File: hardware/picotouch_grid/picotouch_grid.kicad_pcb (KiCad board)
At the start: 2 copper layers, 180 x 110 mm, 127 parts, among them U1 Pico, U2 TS20, U3 TS20

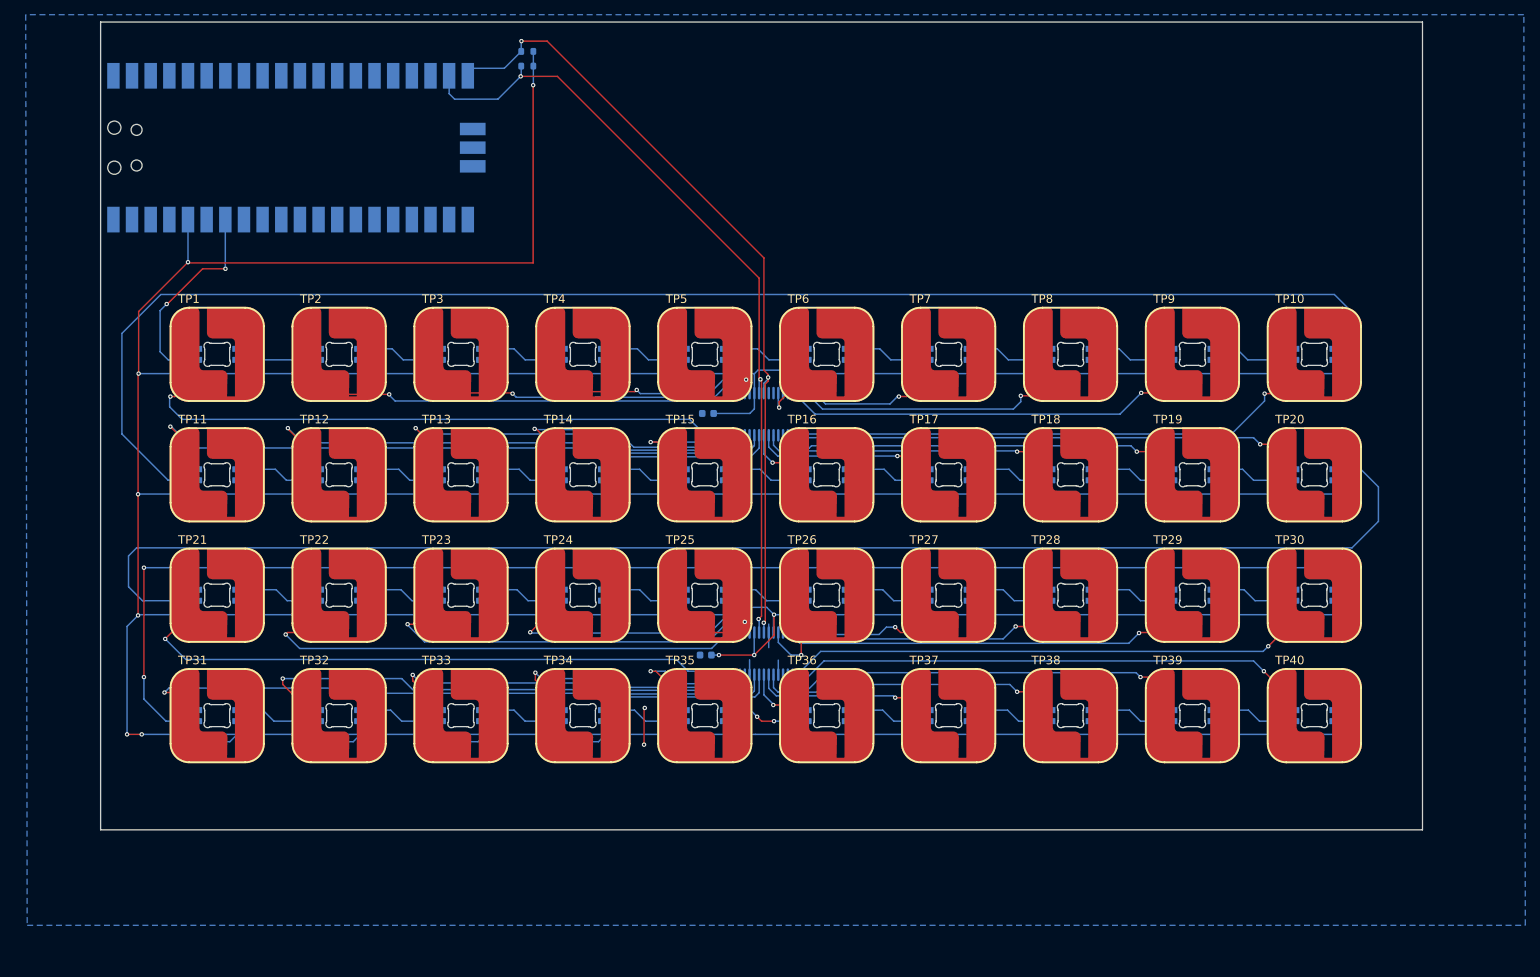
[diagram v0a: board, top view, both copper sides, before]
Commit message: added jlcpcb dru rules from "KiCad-DesignRules"
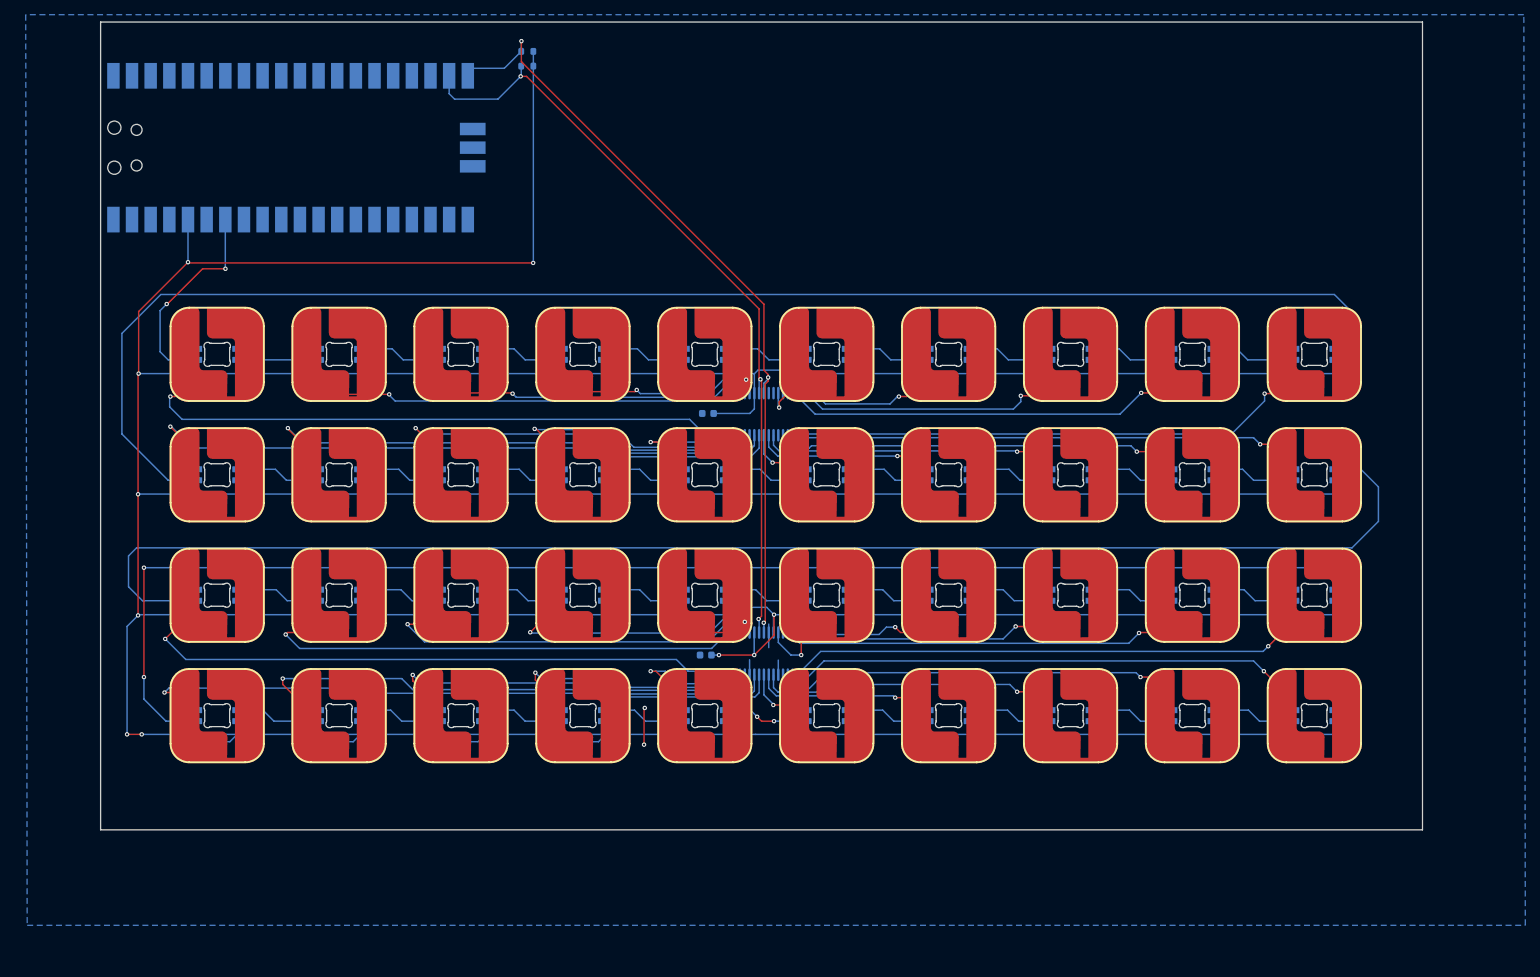
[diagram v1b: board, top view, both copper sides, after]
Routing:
- net /TOUCH_SDA: track 108.7 -> 106.3 mm
- net /TOUCH_SCL: track 110.7 -> 108.6 mm

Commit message: pcb: added midi in/out, pwm audio out
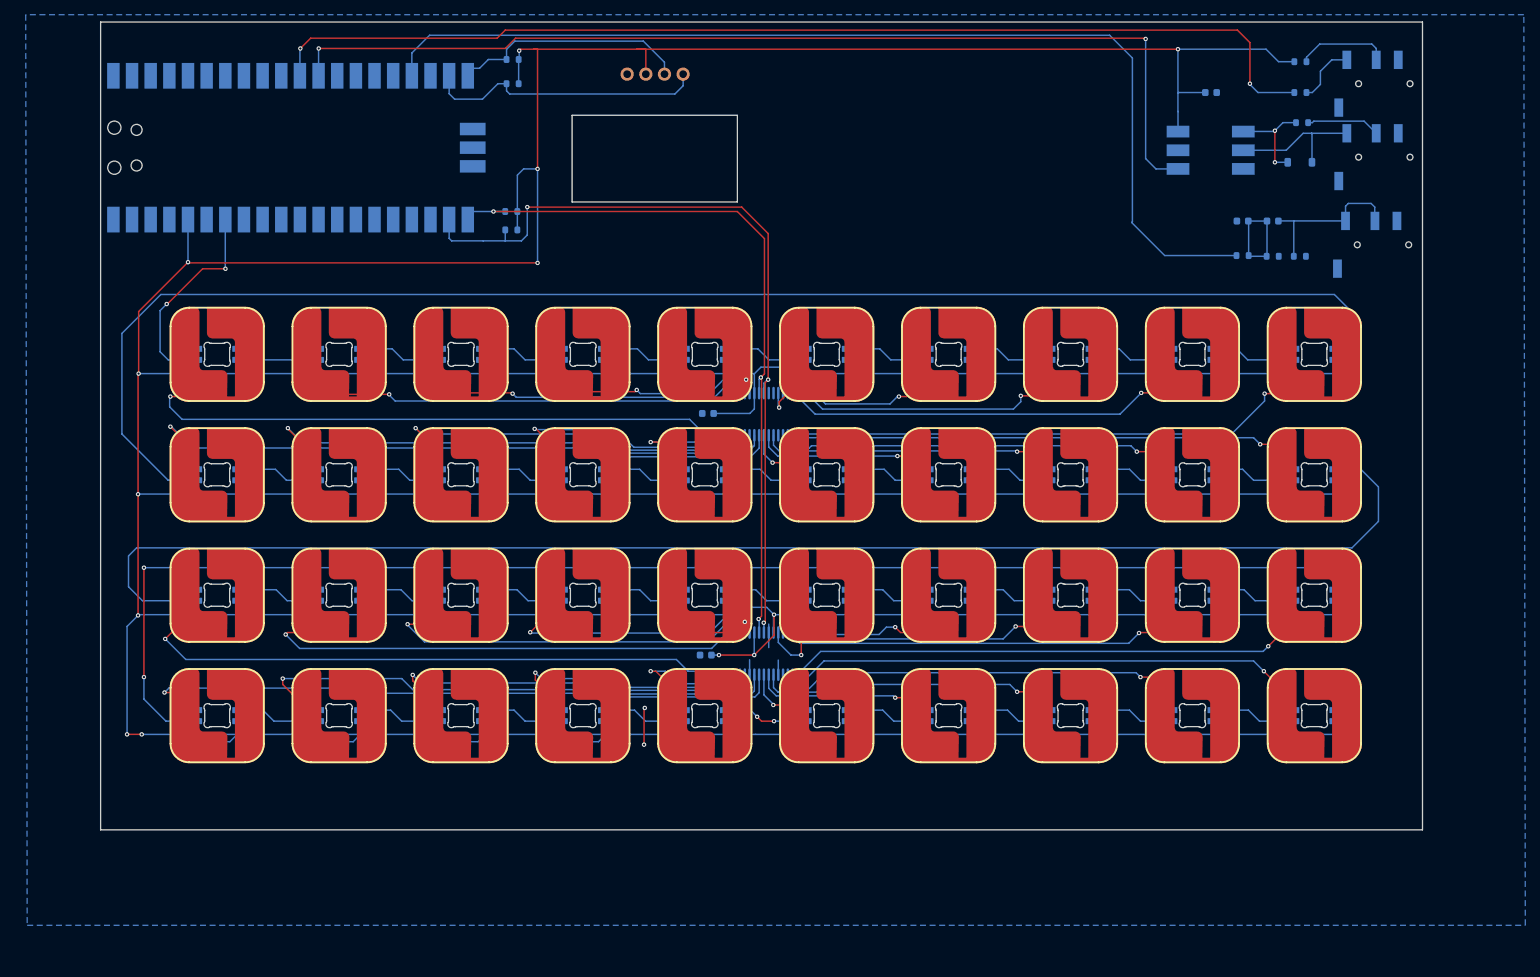
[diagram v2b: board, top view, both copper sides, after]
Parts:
- added C43: 100n, Capacitor_SMD:C_0603_1608Metric, B.Cu at (188.2, 34.6)
- added C44: 100n, Capacitor_SMD:C_0603_1608Metric, B.Cu at (192.5, 52.1)
- added C45: 47uF, Capacitor_SMD:C_0603_1608Metric, B.Cu at (196.6, 52.1)
- added D1: 1N4148, Diode_SMD:D_SOD-123, B.Cu at (200.3, 44.1)
- added DISP1: HS96L03W2C03, todbot_stuff:OLED-TH_under_L27.8-W27.2-P2.54_C9900033791, F.Cu at (112.5, 32.1)
- added J1: TRRS, Keebio-Parts:TRRS-PJ-320D, B.Cu at (216.9, 43.4)
- added J2: TRRS, Keebio-Parts:TRRS-PJ-320D, B.Cu at (216.9, 33.4)
- added J3: TRRS, Keebio-Parts:TRRS-PJ-320D, B.Cu at (216.7, 55.3)
- added R10: 1.8k, Resistor_SMD:R_0603_1608Metric, B.Cu at (200.3, 56.9)
- added R3: 4.7k, Resistor_SMD:R_0603_1608Metric, B.Cu at (92.9, 53.3)
- added R4: 4.7k, Resistor_SMD:R_0603_1608Metric, B.Cu at (92.9, 50.8)
- added R5: 200, Resistor_SMD:R_0603_1608Metric, B.Cu at (200.6, 38.7)
- added R6: 33, Resistor_SMD:R_0603_1608Metric, B.Cu at (200.4, 30.4)
- added R7: 10, Resistor_SMD:R_0603_1608Metric, B.Cu at (200.4, 34.6)
- added R8: 200, Resistor_SMD:R_0603_1608Metric, B.Cu at (192.5, 56.8)
- added R9: 100, Resistor_SMD:R_0603_1608Metric, B.Cu at (196.6, 56.9)
- added U5: H11L1, Package_DIP:DIP-6_W8.89mm_SMDSocket_LongPads, B.Cu at (188.2, 42.5)
- moved R1 3.12 mm to (93.1, 33.4)
- moved R2 2.28 mm to (93.1, 30.1)
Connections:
- R1 pad 2: /TOUCH_SDA -> /DISP_SDA
- R2 pad 2: /TOUCH_SCL -> /DISP_SCL
- U1 pad 11: unconnected-(U1-GPIO8-Pad11) -> /MIDI_OUT
- U1 pad 12: unconnected-(U1-GPIO9-Pad12) -> /MIDI_IN
- U1 pad 17: unconnected-(U1-GPIO13-Pad17) -> /PWM_AUDIO
- U1 pad 19: /TOUCH_SDA -> /DISP_SDA
- U1 pad 20: /TOUCH_SCL -> /DISP_SCL
- U1 pad 21: unconnected-(U1-GPIO16-Pad21) -> /TOUCH_SDA
- U1 pad 22: unconnected-(U1-GPIO17-Pad22) -> /TOUCH_SCL
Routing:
- net /MIDI_OUT: track 0.00 -> 147.9 mm, vias 0 -> 2
- net /PWM_AUDIO: track 0.00 -> 143.0 mm
- net +3V3: track 953.7 -> 1096.6 mm, vias 10 -> 13
- net /MIDI_IN: track 0.00 -> 139.1 mm, vias 0 -> 2
- net /DISP_SDA: track 0.00 -> 37.7 mm
- net /DISP_SCL: track 0.00 -> 32.0 mm
- net /AUDIO_OUT: track 0.00 -> 22.2 mm
- net Net-(D1-A): track 0.00 -> 19.2 mm
- net Net-(C44-Pad1): track 0.00 -> 14.6 mm
- net Net-(D1-K): track 0.00 -> 13.7 mm, vias 0 -> 2
- net Net-(J2-RING1): track 0.00 -> 12.6 mm
- net Net-(J1-RING1): track 0.00 -> 10.0 mm
- net Net-(J2-TIP): track 0.00 -> 8.40 mm
- net /TOUCH_SDA: track 106.3 -> 99.9 mm
- net /TOUCH_SCL: track 108.6 -> 110.9 mm
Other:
- outline, holes or cut-outs redrawn

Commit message: pcb: add more buttons, clean up layout of sch & pcb
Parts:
- added H1: MountingHole, MountingHole:MountingHole_2.7mm_M2.5, F.Cu at (34.0, 34.0)
- added H2: MountingHole, MountingHole:MountingHole_2.7mm_M2.5, F.Cu at (34.0, 136.0)
- added H3: MountingHole, MountingHole:MountingHole_2.7mm_M2.5, F.Cu at (206.0, 34.0)
- added H4: MountingHole, MountingHole:MountingHole_2.7mm_M2.5, F.Cu at (206.0, 136.0)
- added R11: 1M, Resistor_SMD:R_0603_1608Metric, B.Cu at (47.1, 33.6)
- added R12: 1M, Resistor_SMD:R_0603_1608Metric, B.Cu at (49.9, 33.6)
- added R13: 1M, Resistor_SMD:R_0603_1608Metric, B.Cu at (52.6, 33.6)
- added R14: 1M, Resistor_SMD:R_0603_1608Metric, B.Cu at (127.2, 39.2)
- added R15: 1M, Resistor_SMD:R_0603_1608Metric, B.Cu at (138.2, 39.2)
- added R16: 1M, Resistor_SMD:R_0603_1608Metric, B.Cu at (149.2, 39.2)
- added R17: 1M, Resistor_SMD:R_0603_1608Metric, B.Cu at (160.4, 39.2)
- added SLIDER1: ~, todbot_eagle2023:TOUCHSLIDER3_8x40B, F.Cu at (56.6, 40.4)
- added TP41: Capacitive Button, SparkFun-Switch:Pad-CapacitiveTouch, F.Cu at (127.2, 42.7)
- added TP42: Capacitive Button, SparkFun-Switch:Pad-CapacitiveTouch, F.Cu at (138.2, 42.7)
- added TP43: Capacitive Button, SparkFun-Switch:Pad-CapacitiveTouch, F.Cu at (149.2, 42.7)
- added TP44: Capacitive Button, SparkFun-Switch:Pad-CapacitiveTouch, F.Cu at (160.2, 42.7)
- added rx1: rx, TestPoint:TestPoint_Pad_D2.0mm, B.Cu at (43.4, 32.8)
- added tx1: tx, TestPoint:TestPoint_Pad_D2.0mm, B.Cu at (39.4, 32.8)
- moved R8 11.1 mm to (185.5, 65.4)
- moved C43 11.1 mm to (181.2, 43.2)
- moved C44 11.1 mm to (185.5, 60.7)
- moved C45 11.1 mm to (189.6, 60.7)
- moved D1 11.1 mm to (193.3, 52.7)
- moved J2 11.1 mm to (209.9, 42.0)
- moved J3 11.1 mm to (209.7, 63.9)
- moved R10 11.1 mm to (193.3, 65.5)
- moved R9 11.1 mm to (189.6, 65.5)
- moved U5 11.1 mm to (181.2, 51.1)
- moved J1 11.1 mm to (209.9, 52.0)
- moved R5 11.1 mm to (193.6, 47.3)
- moved U1 10.9 mm to (55.8, 50.4)
- moved R6 9.35 mm to (193.4, 36.6)
- moved R7 9.09 mm to (193.4, 40.4)
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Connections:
- U1 pad 1: unconnected-(U1-GPIO0-Pad1) -> /UART_TX
- U1 pad 2: unconnected-(U1-GPIO1-Pad2) -> /UART_RX
- U1 pad 4: unconnected-(U1-GPIO2-Pad4) -> /FADER1A
- U1 pad 5: unconnected-(U1-GPIO3-Pad5) -> /FADER1B
- U1 pad 6: unconnected-(U1-GPIO4-Pad6) -> /FADER1C
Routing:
- net /FADER1C: track 0.00 -> 51.2 mm, vias 0 -> 1
- net /FADER1A: track 0.00 -> 24.3 mm, vias 0 -> 1
- net /FADER1B: track 0.00 -> 16.4 mm, vias 0 -> 1
- net /UART_RX: track 0.00 -> 14.2 mm
- net /UART_TX: track 0.00 -> 13.5 mm
- net Net-(TP42-A): track 0.00 -> 6.94 mm, vias 0 -> 1
- net Net-(TP44-A): track 0.00 -> 6.80 mm, vias 0 -> 1
- net Net-(TP43-A): track 0.00 -> 6.72 mm, vias 0 -> 1
- net /MIDI_IN: track 139.1 -> 145.6 mm
- net Net-(LED10-DOUT): track 204.5 -> 198.2 mm
- net /PWM_AUDIO: track 143.0 -> 147.6 mm
- net /DISP_SCL: track 32.0 -> 36.3 mm
- net /MIDI_OUT: track 147.9 -> 151.5 mm
- net /NEOPIXEL_DATA: track 30.0 -> 26.7 mm
- net /TOUCH_SDA: track 99.9 -> 102.4 mm
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
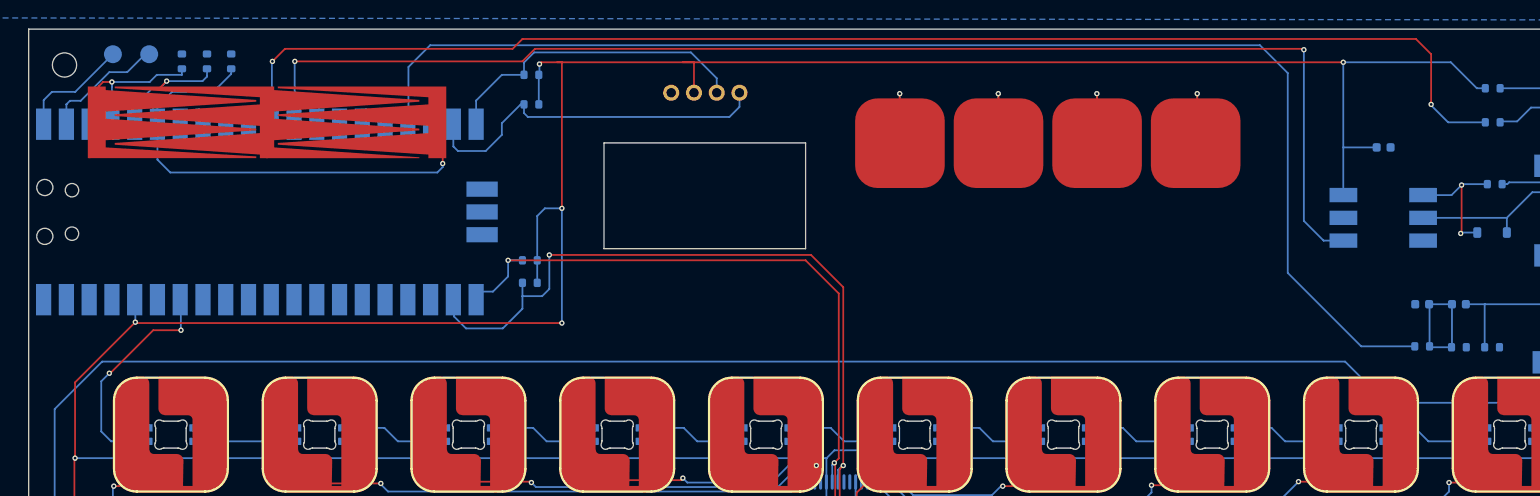
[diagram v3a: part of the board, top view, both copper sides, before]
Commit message: pcb: tune button layout
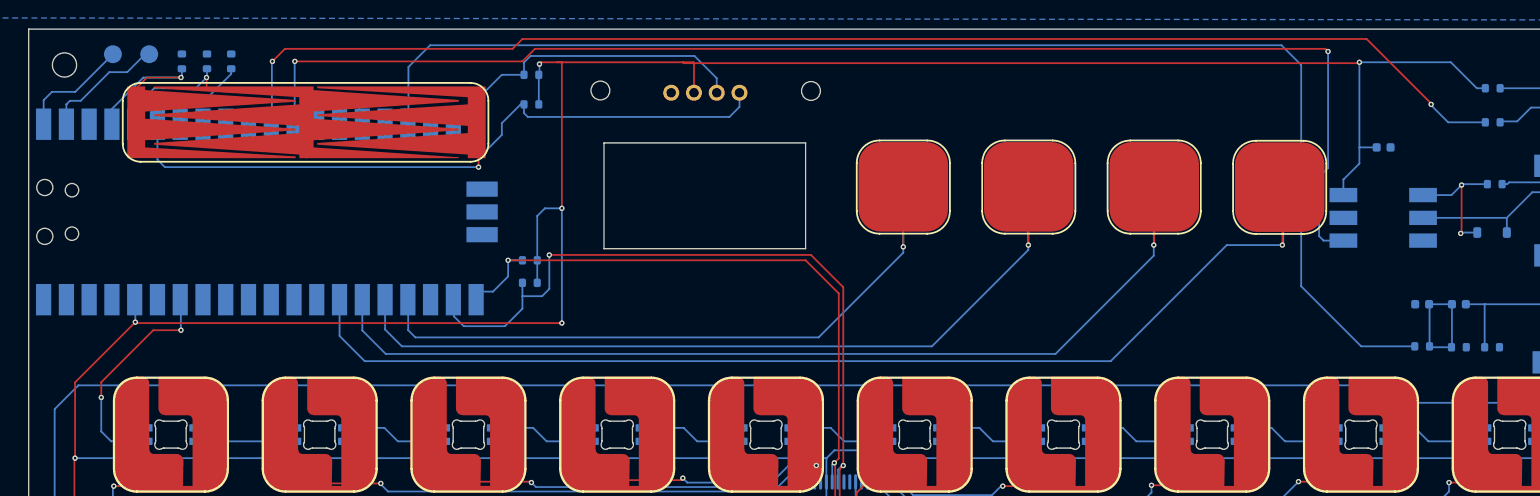
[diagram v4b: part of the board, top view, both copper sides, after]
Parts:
- added H5: MountingHole, MountingHole:MountingHole_2.1mm, F.Cu at (93.8, 36.9)
- added H6: MountingHole, MountingHole:MountingHole_2.1mm, F.Cu at (117.3, 36.9)
- moved R17 15.3 mm to (170.0, 51.1), turned to -90 degrees
- moved R16 13.4 mm to (155.6, 51.0), turned to -90 degrees
- moved R15 12.3 mm to (141.5, 51.1), turned to -90 degrees
- moved R14 11.9 mm to (127.6, 51.1), turned to -90 degrees
- moved TP44 10.6 mm to (169.6, 47.6)
- moved TP43 8.02 mm to (155.6, 47.6)
- moved TP42 5.93 mm to (141.6, 47.6)
- moved TP41 4.88 mm to (127.6, 47.6)
- moved SLIDER1 4.40 mm to (61.0, 40.4)
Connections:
- R14 pad 2: Net-(TP41-A) -> /BUT1
- R15 pad 2: Net-(TP42-A) -> /BUT2
- R16 pad 2: Net-(TP43-A) -> /BUT3
- R17 pad 2: Net-(TP44-A) -> /BUT4
- TP41 pad 1: Net-(TP41-A) -> /BUT1
- TP42 pad 1: Net-(TP42-A) -> /BUT2
- TP43 pad 1: Net-(TP43-A) -> /BUT3
- TP44 pad 1: Net-(TP44-A) -> /BUT4
- U1 pad 24: unconnected-(U1-GPIO18-Pad24) -> /BUT1
- U1 pad 25: unconnected-(U1-GPIO19-Pad25) -> /BUT2
- U1 pad 26: unconnected-(U1-GPIO20-Pad26) -> /BUT3
- U1 pad 27: unconnected-(U1-GPIO21-Pad27) -> /BUT4
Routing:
- net /BUT4: track 0.00 -> 125.4 mm, vias 0 -> 1
- net /BUT3: track 0.00 -> 108.4 mm, vias 0 -> 1
- net /BUT2: track 0.00 -> 90.5 mm, vias 0 -> 1
- net /BUT1: track 0.00 -> 76.7 mm, vias 0 -> 1
- net Net-(TP42-A): track 6.94 -> 0.00 mm, vias 1 -> 0
- net Net-(TP44-A): track 6.80 -> 0.00 mm, vias 1 -> 0
- net Net-(TP43-A): track 6.72 -> 0.00 mm, vias 1 -> 0
- net /FADER1C: track 51.2 -> 54.8 mm
- net /MIDI_OUT: track 151.5 -> 148.3 mm
- net /MIDI_IN: track 145.6 -> 147.9 mm
- net Net-(LED10-DOUT): track 198.2 -> 196.0 mm
- net Net-(TP41-A): track 2.16 -> 0.00 mm, vias 1 -> 0
- net /FADER1B: track 16.4 -> 14.4 mm
- net /FADER1A: track 24.3 -> 26.2 mm
- net /PWM_AUDIO: track 147.6 -> 149.0 mm
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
